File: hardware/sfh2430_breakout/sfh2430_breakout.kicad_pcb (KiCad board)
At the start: 2 copper layers, 76.5 x 65.6 mm, 22 parts, among them J2 Conn_01x10, U1 LTC2052IS_PBF

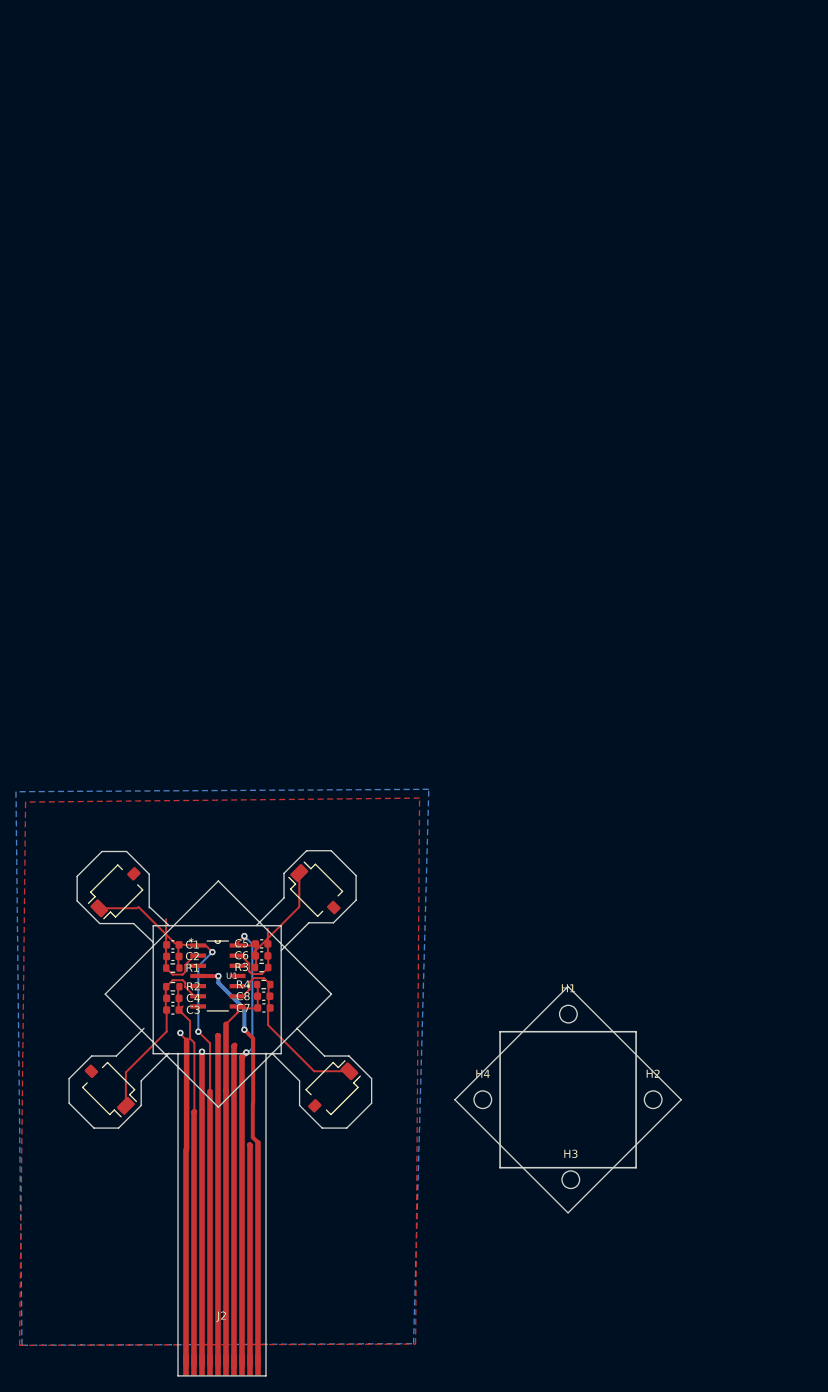
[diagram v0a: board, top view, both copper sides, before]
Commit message: add PiCoral 1.0.0
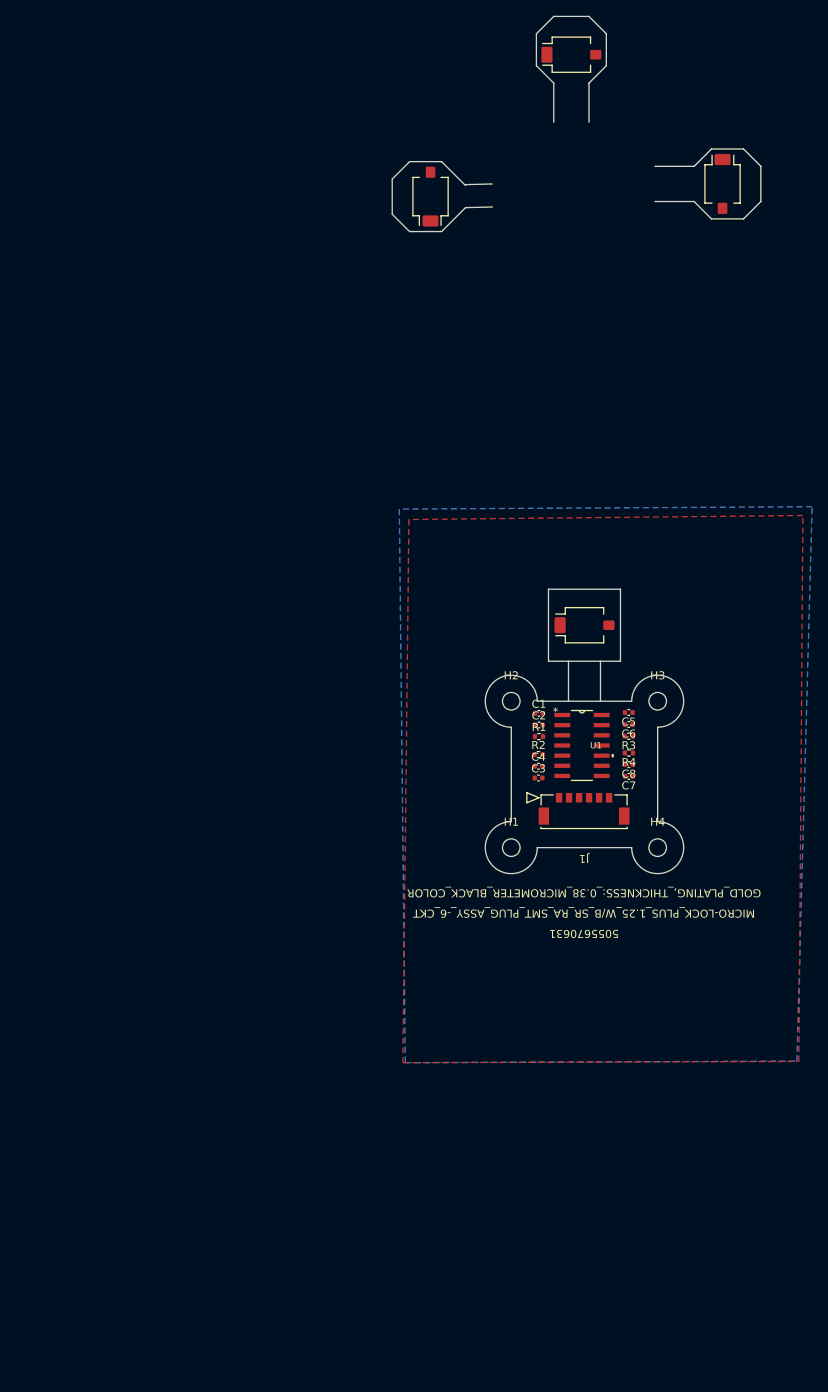
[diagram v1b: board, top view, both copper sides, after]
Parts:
- removed J2: Conn_01x10, adcs:10pin_1mm_pitch_flat_flex
- added J1: 5055670631, adcs:CON_5055670631, F.Cu at (127.5, 89.3)
- C1, C2, C3, C4, C5, C6, C7, C8: footprint Capacitor_SMD:C_0603_1608Metric -> Capacitor_SMD:C_0402_1005Metric
- R1, R2, R3, R4: footprint Resistor_SMD:R_0603_1608Metric -> Resistor_SMD:R_0402_1005Metric
- moved D4 123.2 mm to (148.0, 12.5), turned to -90 degrees
- moved D3 109.2 mm to (129.1, -3.62), turned to 0 degrees
- moved D1 95.3 mm to (111.5, 14.1), turned to 90 degrees
- moved D2 83.0 mm to (130.7, 67.7), turned to 0 degrees
- moved H3 60.8 mm to (139.9, 77.2)
- moved C6 54.2 mm to (136.2, 80.1)
- moved C5 54.2 mm to (136.2, 78.6)
- moved R3 54.2 mm to (136.2, 81.6)
- moved C2 54.1 mm to (125.0, 80.2)
- moved R1 54.1 mm to (125.0, 81.6)
- moved C1 54.1 mm to (125.0, 78.7)
- moved C3 54.1 mm to (125.0, 86.8)
- moved C4 54.1 mm to (125.0, 85.3)
- moved R2 54.1 mm to (125.0, 83.9)
- moved C8 54.0 mm to (136.3, 85.1)
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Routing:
- net GND: track 191.0 -> 0.00 mm, vias 2 -> 0
- net /OUT4: track 62.0 -> 0.00 mm, vias 2 -> 0
- net /OUT1: track 61.9 -> 0.00 mm, vias 2 -> 0
- net +3V3: track 53.2 -> 0.00 mm, vias 2 -> 0
- net /OUT3: track 50.8 -> 0.00 mm
- net /OUT2: track 48.8 -> 0.00 mm
- net /Photodiode 3/IN-: track 23.6 -> 0.00 mm
- net /Photodiode 1/IN-: track 23.2 -> 0.00 mm
- net /Photodiode 4/IN-: track 23.1 -> 0.00 mm
- net /Photodiode 2/IN-: track 22.6 -> 0.00 mm
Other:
- board size 76.5 x 65.6 mm -> 46.1 x 107.2 mm
